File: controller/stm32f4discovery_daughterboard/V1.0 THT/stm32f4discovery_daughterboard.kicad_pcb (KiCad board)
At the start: 2 copper layers, 99.9 x 70 mm, 144 parts, among them P1 CONN_25X2, P2 CONN_25X2, T1 BC547

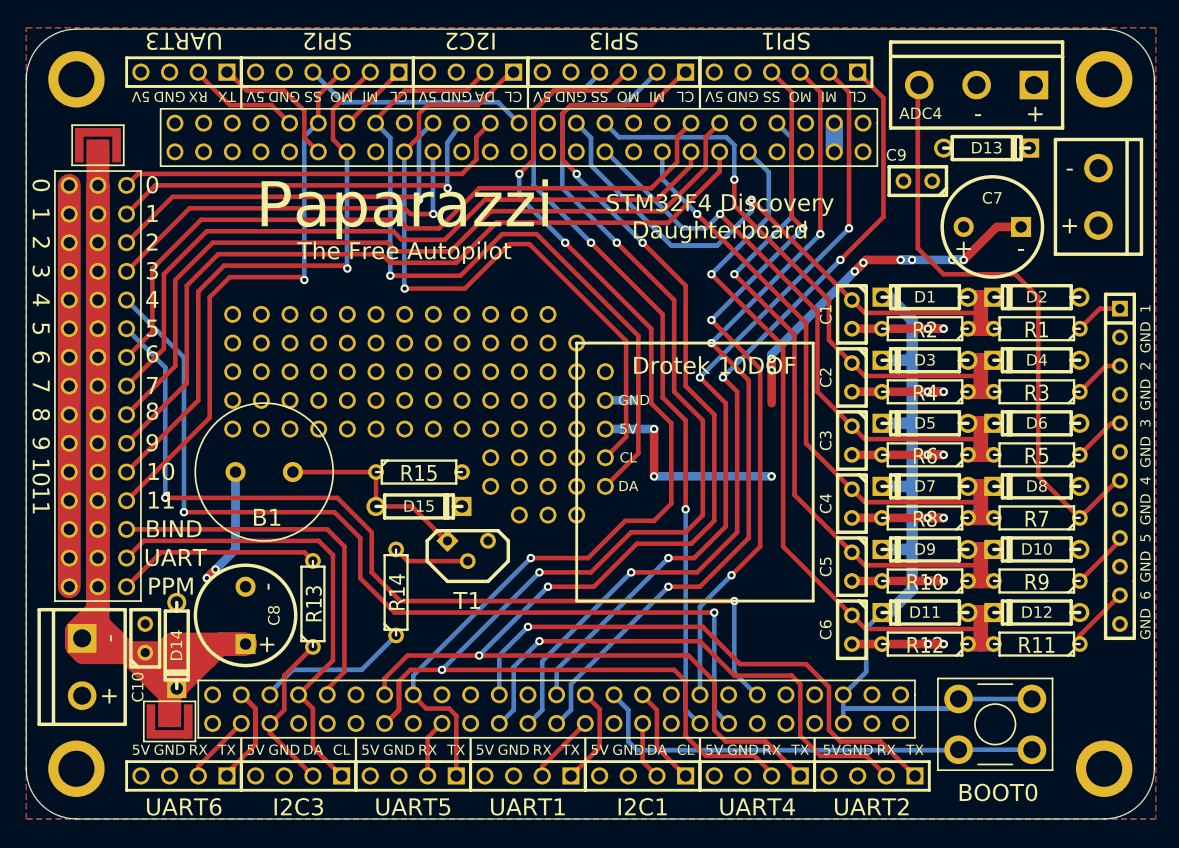
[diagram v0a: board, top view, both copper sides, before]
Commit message: fixed align of the main header
The Main pin header (for the dosvocery board) was offset in the previous
version.
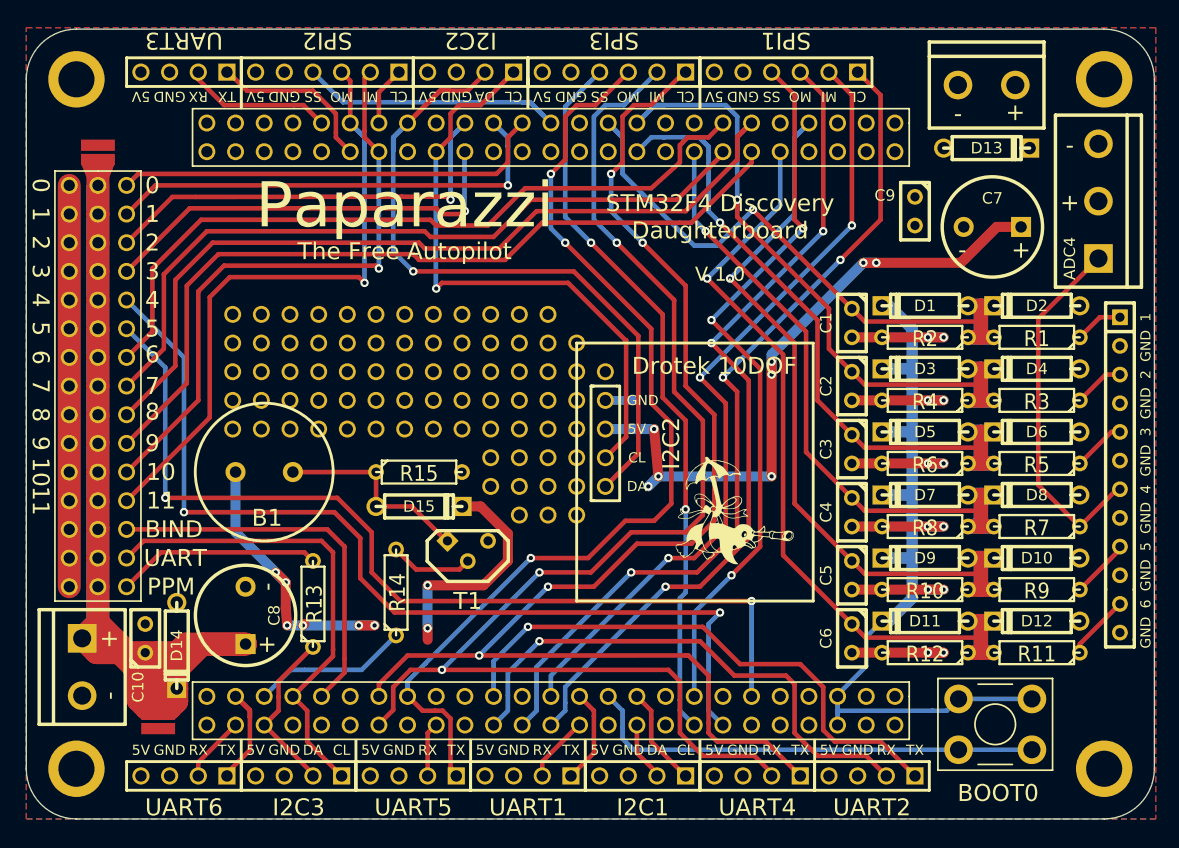
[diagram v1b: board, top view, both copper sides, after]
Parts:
- added VAL: paparazzi_11mm, paparazzi_11mm, F.Cu at (156.2, 116.5)
- JP1, JP2: footprint Ujumper -> Solder_Jumper_big
- moved screw1 14.9 mm to (188.5, 89.0), turned to 90 degrees
- moved screw2 14.0 mm to (178.6, 78.7), turned to 180 degrees
- moved P1 2.83 mm to (170.4, 83.4)
- moved C9 2.68 mm to (172.2, 89.9), turned to 270 degrees
- moved JP1 0.97 mm to (105.3, 135.0)
- moved ADC1 0.76 mm to (190.4, 113.3)
- moved C1 0.76 mm to (166.6, 99.8)
- moved C2 0.76 mm to (166.6, 105.4)
- moved C3 0.76 mm to (166.6, 111.0)
- moved C4 0.76 mm to (166.6, 116.6)
- moved C5 0.76 mm to (166.6, 122.2)
- moved C6 0.76 mm to (166.6, 127.8)
- moved D1 0.76 mm to (173.1, 98.3)
- moved D10 0.76 mm to (183.0, 120.7)
- moved D11 0.76 mm to (173.1, 126.2)
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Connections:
- screw1 pad 1: 5V -> ADC4
- screw1 pad 2: GND -> 5V
- screw1 pad 3: ADC4 -> GND
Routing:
- net 5V: track 66.1 -> 111.5 mm, vias 13 -> 16
- net PWM_VIN: track 179.7 -> 138.2 mm
- net ADC4: track 53.0 -> 32.4 mm
- net PB10: track 61.9 -> 53.5 mm
- net PC11: track 128.3 -> 120.0 mm
- net PE11: track 35.8 -> 43.5 mm
- net PB15: track 50.1 -> 57.6 mm
- net PE7: track 20.1 -> 26.3 mm
- net PC10: track 125.9 -> 119.8 mm
- net PE13: track 35.0 -> 40.7 mm
- net PC5: track 62.6 -> 66.5 mm
- net PA1: track 70.0 -> 73.9 mm
- net PC1: track 71.7 -> 75.2 mm
- net PE3: track 67.8 -> 64.4 mm
- net PD9: track 10.0 -> 13.2 mm
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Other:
- board text added: "V 1.0"
